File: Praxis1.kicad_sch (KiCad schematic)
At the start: 44 parts, among them J10 Conn_01x02, J11 Conn_01x02, J12 Conn_01x02, J13 Conn_01x02

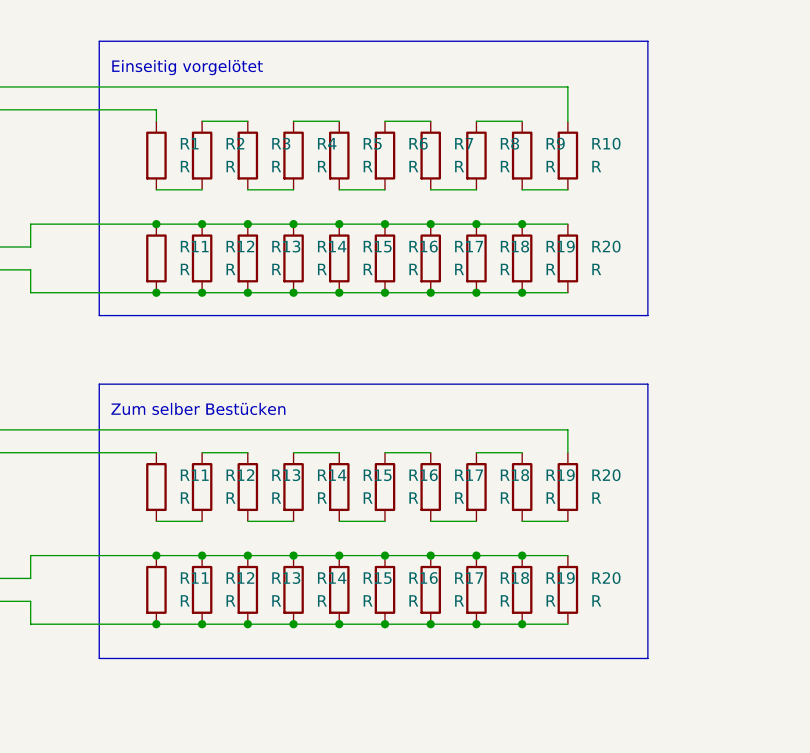
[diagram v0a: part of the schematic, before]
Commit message: Resolves #2: Added current limiting resistor values (i.e. 620 Ohm)
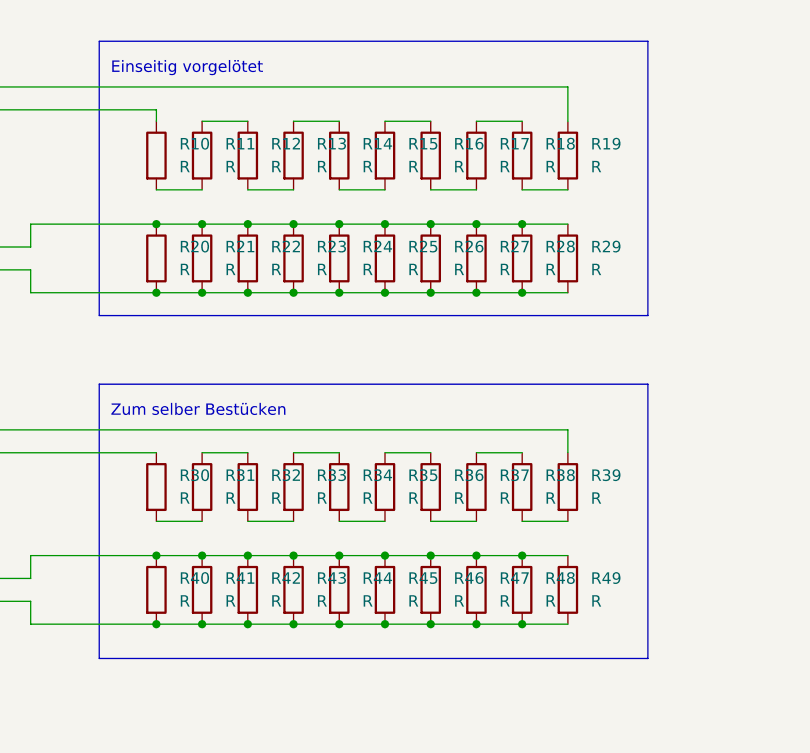
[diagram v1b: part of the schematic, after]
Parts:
- renumbered R1 to R10, R2 to R11, R3 to R12, R4 to R13, R5 to R14, R6 to R15, R7 to R16, R8 to R17, R9 to R18, R10 to R19, R11 to R20, R12 to R21, R13 to R22, R14 to R23, R15 to R24, R16 to R25, R17 to R26, R18 to R27, R19 to R28, R20 to R29, R11 to R30, R12 to R31, R13 to R32, R14 to R33, R15 to R34, R16 to R35, R17 to R36, R18 to R37, R19 to R38, R20 to R39, R11 to R40, R12 to R41, R13 to R42, R14 to R43, R15 to R44, R16 to R45, R17 to R46, R18 to R47, R19 to R48, R20 to R49
